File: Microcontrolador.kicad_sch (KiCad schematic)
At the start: 2 parts, among them J2 Conn_01x15, J3 Conn_01x15

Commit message: Inicio de trazado de PCB
Se empezaron a acomodar los footprints.
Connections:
- net Analog_Ilum: now also J2.4 (Pin_4); no longer J2.2 (Pin_2)
- net Analog_pH: now also J2.2 (Pin_2); no longer J2.4 (Pin_4)
- no-connect marks 12 -> 11
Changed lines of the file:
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@@
   (no_connect (at 243.84 97.155))
   (no_connect (at 243.84 92.075))
-  (no_connect (at 243.84 109.855))
   (no_connect (at 215.9 84.455))
   (no_connect (at 243.84 94.615))
@@
     (stroke (width 0) (type default) (color 0 0 0 0))
   )
+  (wire (pts (xy 212.09 76.835) (xy 215.9 76.835))
+    (stroke (width 0) (type default) (color 0 0 0 0))
+  )
+  (wire (pts (xy 109.855 78.74) (xy 128.6002 78.7146))
+    (stroke (width 0) (type default) (color 0 0 0 0))
+  )
+  (wire (pts (xy 215.9 89.535) (xy 200.66 89.535))
+    (stroke (width 0) (type default) (color 0 0 0 0))
+  )
+  (wire (pts (xy 212.09 79.375) (xy 215.9 79.375))
+    (stroke (width 0) (type default) (color 0 0 0 0))
+  )
+  (wire (pts (xy 109.855 69.215) (xy 130.175 69.215))
+    (stroke (width 0) (type default) (color 0 0 0 0))
+  )
+  (wire (pts (xy 208.28 107.315) (xy 215.9 107.315))
+    (stroke (width 0) (type default) (color 0 0 0 0))
+  )
+  (wire (pts (xy 215.9 92.075) (xy 200.66 92.075))
+    (stroke (width 0) (type default) (color 0 0 0 0))
+  )
+  (wire (pts (xy 109.22 118.745) (xy 124.46 118.745))
+    (stroke (width 0) (type default) (color 0 0 0 0))
+  )
+  (wire (pts (xy 109.22 132.715) (xy 121.285 132.715))
+    (stroke (width 0) (type default) (color 0 0 0 0))
+  )
+  (wire (pts (xy 215.9 104.775) (xy 200.66 104.775))
+    (stroke (width 0) (type default) (color 0 0 0 0))
+  )
+  (wire (pts (xy 113.665 59.69) (xy 109.855 59.69))
+    (stroke (width 0) (type default) (color 0 0 0 0))
+  )
+  (wire (pts (xy 59.055 148.59) (xy 62.865 148.59))
+    (stroke (width 0) (type default) (color 0 0 0 0))
+  )
+  (wire (pts (xy 113.665 57.785) (xy 109.855 57.785))
+    (stroke (width 0) (type default) (color 0 0 0 0))
+  )
+  (wire (pts (xy 247.65 99.695) (xy 243.84 99.695))
+    (stroke (width 0) (type default) (color 0 0 0 0))
+  )
+  (wire (pts (xy 59.055 146.685) (xy 62.865 146.685))
+    (stroke (width 0) (type default) (color 0 0 0 0))
+  )
+  (wire (pts (xy 243.84 74.295) (xy 262.5852 74.2696))
+    (stroke (width 0) (type default) (color 0 0 0 0))
+  )
+  (wire (pts (xy 243.84 76.835) (xy 260.35 76.835))
+    (stroke (width 0) (type default) (color 0 0 0 0))
+  )
+  (wire (pts (xy 113.665 55.88) (xy 109.855 55.88))
+    (stroke (width 0) (type default) (color 0 0 0 0))
+  )
+  (wire (pts (xy 109.22 116.84) (xy 124.46 116.84))
+    (stroke (width 0) (type default) (color 0 0 0 0))
+  )
+  (wire (pts (xy 113.665 61.595) (xy 109.855 61.595))
+    (stroke (width 0) (type default) (color 0 0 0 0))
+  )
+  (wire (pts (xy 109.22 120.65) (xy 124.46 120.65))
+    (stroke (width 0) (type default) (color 0 0 0 0))
+  )
+  (wire (pts (xy 215.9 102.235) (xy 200.66 102.235))
+    (stroke (width 0) (type default) (color 0 0 0 0))
+  )
+  (wire (pts (xy 243.84 84.455) (xy 260.35 84.455))
+    (stroke (width 0) (type default) (color 0 0 0 0))
+  )
+  (wire (pts (xy 109.855 76.835) (xy 126.365 76.835))
+    (stroke (width 0) (type default) (color 0 0 0 0))
+  )
+  (wire (pts (xy 59.055 118.745) (xy 62.865 118.745))
+    (stroke (width 0) (type default) (color 0 0 0 0))
+  )
+  (wire (pts (xy 59.055 132.715) (xy 62.865 132.715))
+    (stroke (width 0) (type default) (color 0 0 0 0))
+  )
+  (wire (pts (xy 109.22 124.46) (xy 124.46 124.46))
+    (stroke (width 0) (type default) (color 0 0 0 0))
+  )
+  (wire (pts (xy 59.055 124.46) (xy 62.865 124.46))
+    (stroke (width 0) (type default) (color 0 0 0 0))
+  )
+  (wire (pts (xy 109.22 122.555) (xy 124.46 122.555))
+    (stroke (width 0) (type default) (color 0 0 0 0))
+  )
+  (polyline (pts (xy 176.9618 12.0396) (xy 176.9618 166.0144))
+    (stroke (width 0) (type default) (color 0 0 0 0))
+  )
+  (wire (pts (xy 59.055 116.84) (xy 62.865 116.84))
+    (stroke (width 0) (type default) (color 0 0 0 0))
+  )
+  (wire (pts (xy 109.22 140.97) (xy 122.1486 140.97))
+    (stroke (width 0) (type default) (color 0 0 0 0))
+  )
+  (wire (pts (xy 215.9 94.615) (xy 200.66 94.615))
+    (stroke (width 0) (type default) (color 0 0 0 0))
+  )
+  (wire (pts (xy 59.055 120.65) (xy 62.865 120.65))
+    (stroke (width 0) (type default) (color 0 0 0 0))
+  )
+  (wire (pts (xy 109.22 139.065) (xy 121.285 139.065))
+    (stroke (width 0) (type default) (color 0 0 0 0))
+  )
+  (wire (pts (xy 59.055 150.495) (xy 62.865 150.495))
+    (stroke (width 0) (type default) (color 0 0 0 0))
+  )
+  (wire (pts (xy 59.055 139.065) (xy 62.865 139.065))
+    (stroke (width 0) (type default) (color 0 0 0 0))
+  )
   (wire (pts (xy 212.09 81.915) (xy 215.9 81.915))
-    (stroke (width 0) (type default) (color 0 0 0 0))
-  )
-  (wire (pts (xy 109.855 78.74) (xy 128.6002 78.7146))
-    (stroke (width 0) (type default) (color 0 0 0 0))
-  )
-  (wire (pts (xy 215.9 89.535) (xy 200.66 89.535))
-    (stroke (width 0) (type default) (color 0 0 0 0))
-  )
-  (wire (pts (xy 212.09 79.375) (xy 215.9 79.375))
-    (stroke (width 0) (type default) (color 0 0 0 0))
-  )
-  (wire (pts (xy 109.855 69.215) (xy 130.175 69.215))
-    (stroke (width 0) (type default) (color 0 0 0 0))
-  )
-  (wire (pts (xy 208.28 107.315) (xy 215.9 107.315))
-    (stroke (width 0) (type default) (color 0 0 0 0))
-  )
-  (wire (pts (xy 215.9 92.075) (xy 200.66 92.075))
-    (stroke (width 0) (type default) (color 0 0 0 0))
-  )
-  (wire (pts (xy 109.22 118.745) (xy 124.46 118.745))
-    (stroke (width 0) (type default) (color 0 0 0 0))
-  )
-  (wire (pts (xy 109.22 132.715) (xy 121.285 132.715))
-    (stroke (width 0) (type default) (color 0 0 0 0))
-  )
-  (wire (pts (xy 215.9 104.775) (xy 200.66 104.775))
-    (stroke (width 0) (type default) (color 0 0 0 0))
-  )
-  (wire (pts (xy 113.665 59.69) (xy 109.855 59.69))
-    (stroke (width 0) (type default) (color 0 0 0 0))
-  )
-  (wire (pts (xy 59.055 148.59) (xy 62.865 148.59))
-    (stroke (width 0) (type default) (color 0 0 0 0))
-  )
-  (wire (pts (xy 113.665 57.785) (xy 109.855 57.785))
-    (stroke (width 0) (type default) (color 0 0 0 0))
-  )
-  (wire (pts (xy 247.65 99.695) (xy 243.84 99.695))
-    (stroke (width 0) (type default) (color 0 0 0 0))
-  )
-  (wire (pts (xy 59.055 146.685) (xy 62.865 146.685))
-    (stroke (width 0) (type default) (color 0 0 0 0))
-  )
-  (wire (pts (xy 243.84 74.295) (xy 262.5852 74.2696))
-    (stroke (width 0) (type default) (color 0 0 0 0))
-  )
-  (wire (pts (xy 243.84 76.835) (xy 260.35 76.835))
-    (stroke (width 0) (type default) (color 0 0 0 0))
-  )
-  (wire (pts (xy 113.665 55.88) (xy 109.855 55.88))
-    (stroke (width 0) (type default) (color 0 0 0 0))
-  )
-  (wire (pts (xy 109.22 116.84) (xy 124.46 116.84))
-    (stroke (width 0) (type default) (color 0 0 0 0))
-  )
-  (wire (pts (xy 113.665 61.595) (xy 109.855 61.595))
-    (stroke (width 0) (type default) (color 0 0 0 0))
-  )
-  (wire (pts (xy 109.22 120.65) (xy 124.46 120.65))
-    (stroke (width 0) (type default) (color 0 0 0 0))
-  )
-  (wire (pts (xy 215.9 102.235) (xy 200.66 102.235))
-    (stroke (width 0) (type default) (color 0 0 0 0))
-  )
-  (wire (pts (xy 243.84 84.455) (xy 260.35 84.455))
-    (stroke (width 0) (type default) (color 0 0 0 0))
-  )
-  (wire (pts (xy 109.855 76.835) (xy 126.365 76.835))
-    (stroke (width 0) (type default) (color 0 0 0 0))
-  )
-  (wire (pts (xy 59.055 118.745) (xy 62.865 118.745))
-    (stroke (width 0) (type default) (color 0 0 0 0))
-  )
-  (wire (pts (xy 59.055 132.715) (xy 62.865 132.715))
-    (stroke (width 0) (type default) (color 0 0 0 0))
-  )
-  (wire (pts (xy 109.22 124.46) (xy 124.46 124.46))
-    (stroke (width 0) (type default) (color 0 0 0 0))
-  )
-  (wire (pts (xy 59.055 124.46) (xy 62.865 124.46))
-    (stroke (width 0) (type default) (color 0 0 0 0))
-  )
-  (wire (pts (xy 109.22 122.555) (xy 124.46 122.555))
-    (stroke (width 0) (type default) (color 0 0 0 0))
-  )
-  (polyline (pts (xy 176.9618 12.0396) (xy 176.9618 166.0144))
-    (stroke (width 0) (type default) (color 0 0 0 0))
-  )
-  (wire (pts (xy 59.055 116.84) (xy 62.865 116.84))
-    (stroke (width 0) (type default) (color 0 0 0 0))
-  )
-  (wire (pts (xy 109.22 140.97) (xy 122.1486 140.97))
-    (stroke (width 0) (type default) (color 0 0 0 0))
-  )
-  (wire (pts (xy 215.9 94.615) (xy 200.66 94.615))
-    (stroke (width 0) (type default) (color 0 0 0 0))
-  )
-  (wire (pts (xy 59.055 120.65) (xy 62.865 120.65))
-    (stroke (width 0) (type default) (color 0 0 0 0))
-  )
-  (wire (pts (xy 109.22 139.065) (xy 121.285 139.065))
-    (stroke (width 0) (type default) (color 0 0 0 0))
-  )
-  (wire (pts (xy 59.055 150.495) (xy 62.865 150.495))
-    (stroke (width 0) (type default) (color 0 0 0 0))
-  )
-  (wire (pts (xy 59.055 139.065) (xy 62.865 139.065))
-    (stroke (width 0) (type default) (color 0 0 0 0))
-  )
-  (wire (pts (xy 212.09 76.835) (xy 215.9 76.835))
     (stroke (width 0) (type default) (color 0 0 0 0))
   )
@@
     (effects (font (size 1.27 1.27)) (justify left))
   )
-  (hierarchical_label "Analog_Ilum" (shape input) (at 212.09 76.835 180)
+  (hierarchical_label "Analog_Ilum" (shape input) (at 212.09 81.915 180)
     (effects (font (size 1.27 1.27)) (justify right))
   )
@@
     (effects (font (size 1.27 1.27)) (justify left))
   )
+  (hierarchical_label "+3,3V" (shape input) (at 251.46 109.855 0)
+    (effects (font (size 1.27 1.27)) (justify left))
+  )
   (hierarchical_label "SensorNivel_3_Data" (shape bidirectional) (at 59.055 120.65 180)
     (effects (font (size 1.27 1.27)) (justify right))
@@
     (effects (font (size 1.27 1.27)) (justify left))
   )
-  (hierarchical_label "Analog_pH" (shape input) (at 212.09 81.915 180)
-    (effects (font (size 1.27 1.27)) (justify right))
-  )
+  (hierarchical_label "Analog_pH" (shape input) (at 212.09 76.835 180)
+    (effects (font (size 1.27 1.27)) (justify right))
+  )

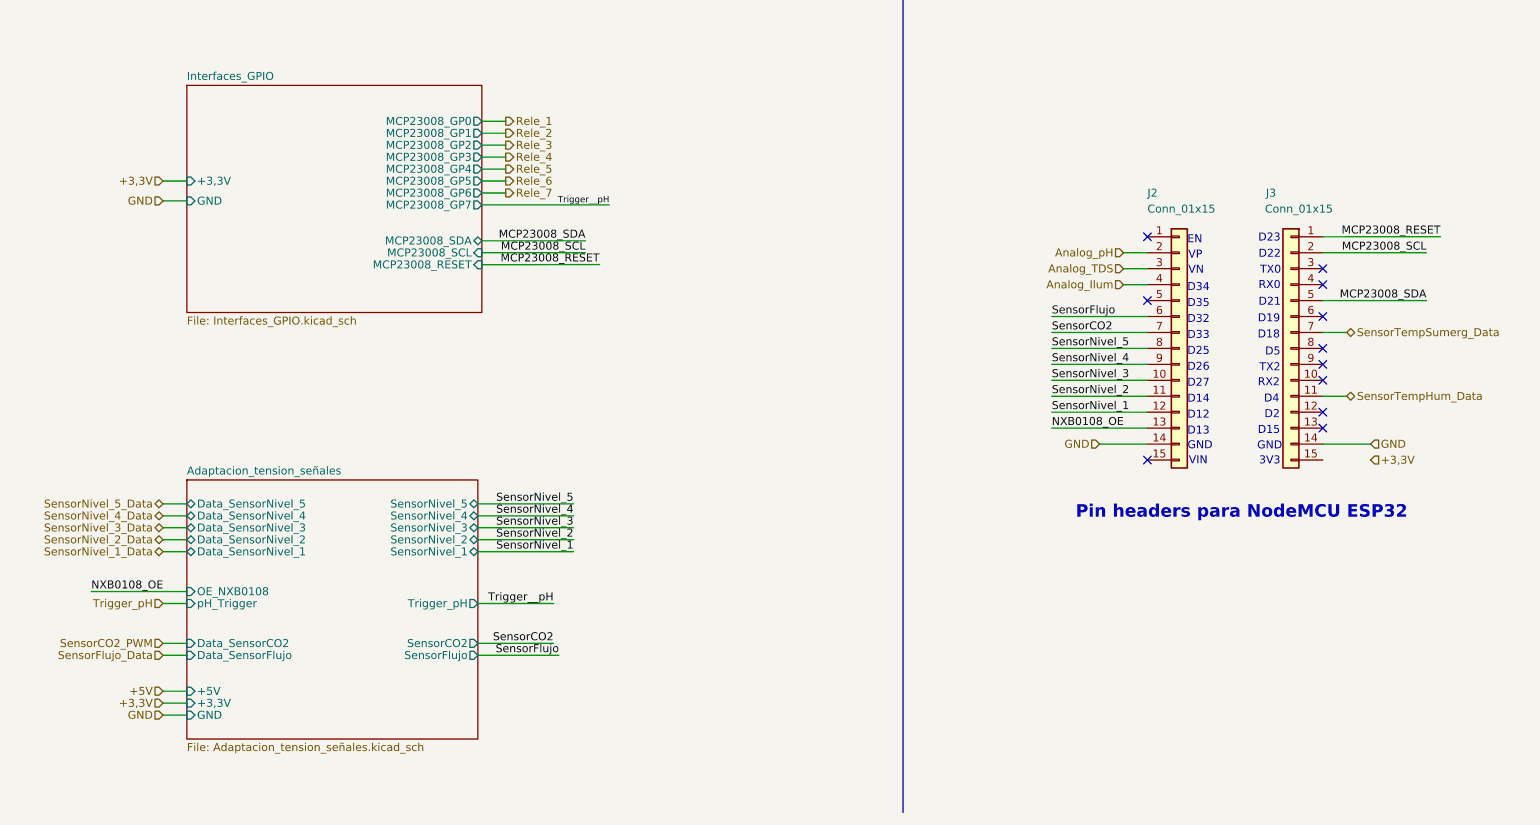
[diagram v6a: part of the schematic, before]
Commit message: Cambios en SCH y PCB.
Se cambio el adaptador de nivel 5-3,3V por un circuito con MOSFET 2N7002, dado que ya no hay stock del NXB. Se modificó el footprint del expansor I/O por uno thorugh-hole.
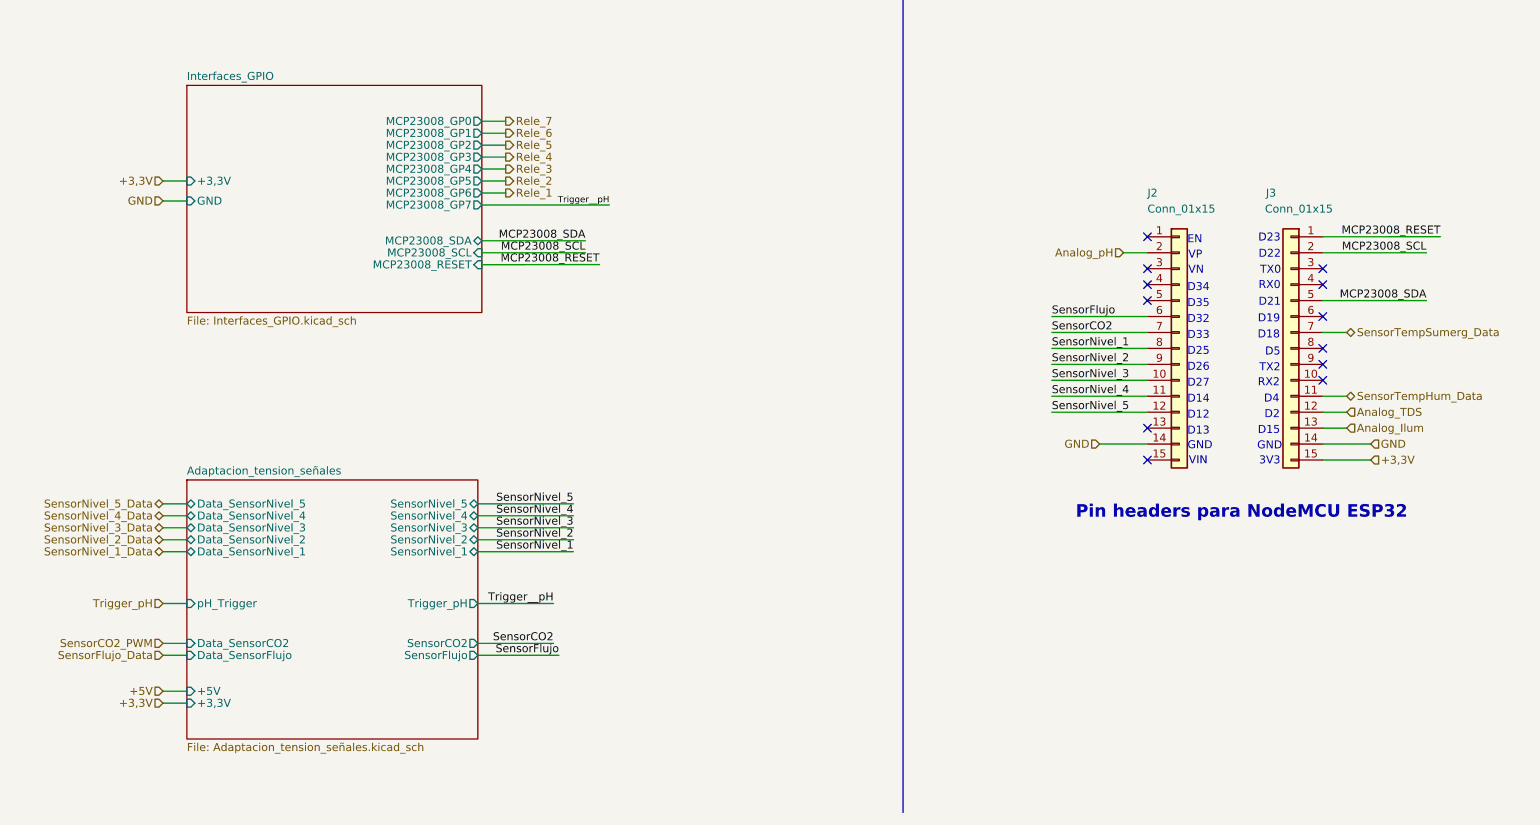
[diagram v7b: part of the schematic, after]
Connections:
- net +3,3V: now also J3.15 (Pin_15)
- net Analog_Ilum: now also J3.13 (Pin_13); no longer J2.4 (Pin_4)
- net Analog_TDS: now also J3.12 (Pin_12); no longer J2.3 (Pin_3)
- net SensorNivel_1: now also J2.8 (Pin_8); no longer J2.12 (Pin_12)
- net SensorNivel_2: now also J2.9 (Pin_9); no longer J2.11 (Pin_11)
- net SensorNivel_4: now also J2.11 (Pin_11); no longer J2.9 (Pin_9)
- net SensorNivel_5: now also J2.12 (Pin_12); no longer J2.8 (Pin_8)
- net NXB0108_OE: no longer names the net of J2.13 (Pin_13)
- no-connect marks 11 -> 12
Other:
- sheet Adaptacion_tension_señales ports: added none; removed GND, OE_NXB0108

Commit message: Finalización de rerouteo de PCB.
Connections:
- net SensorNivel_1: now also J2.12 (Pin_12); no longer J2.8 (Pin_8)
- net SensorNivel_2: now also J2.11 (Pin_11); no longer J2.9 (Pin_9)
- net SensorNivel_4: now also J2.9 (Pin_9); no longer J2.11 (Pin_11)
- net SensorNivel_5: now also J2.8 (Pin_8); no longer J2.12 (Pin_12)
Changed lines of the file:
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@@
     (effects (font (size 1.27 1.27)) (justify right bottom))
   )
-  (label "SensorNivel_4" (at 200.66 99.695 0)
+  (label "SensorNivel_2" (at 200.66 99.695 0)
     (effects (font (size 1.27 1.27)) (justify left bottom))
   )
@@
     (effects (font (size 1.27 1.27)) (justify left bottom))
   )
-  (label "SensorNivel_1" (at 200.66 92.075 0)
+  (label "SensorNivel_5" (at 200.66 92.075 0)
     (effects (font (size 1.27 1.27)) (justify left bottom))
   )
@@
     (effects (font (size 1.27 1.27)) (justify right bottom))
   )
-  (label "SensorNivel_2" (at 200.66 94.615 0)
+  (label "SensorNivel_4" (at 200.66 94.615 0)
     (effects (font (size 1.27 1.27)) (justify left bottom))
   )
@@
     (effects (font (size 1.27 1.27)) (justify right bottom))
   )
-  (label "SensorNivel_5" (at 200.66 102.235 0)
+  (label "SensorNivel_1" (at 200.66 102.235 0)
     (effects (font (size 1.27 1.27)) (justify left bottom))
   )
@@
     (effects (font (size 1.27 1.27)) (justify right))
   )
-  (hierarchical_label "Rele_3" (shape output) (at 113.665 63.5 0)
+  (hierarchical_label "Rele_3" (shape output) (at 113.665 59.69 0)
     (effects (font (size 1.27 1.27)) (justify left))
   )
@@
     (effects (font (size 1.27 1.27)) (justify left))
   )
-  (hierarchical_label "Rele_6" (shape output) (at 113.665 57.785 0)
+  (hierarchical_label "Rele_6" (shape output) (at 113.665 65.405 0)
     (effects (font (size 1.27 1.27)) (justify left))
   )
@@
     (effects (font (size 1.27 1.27)) (justify right))
   )
-  (hierarchical_label "Rele_1" (shape output) (at 113.665 67.31 0)
+  (hierarchical_label "Rele_1" (shape output) (at 113.665 55.88 0)
     (effects (font (size 1.27 1.27)) (justify left))
   )
@@
     (effects (font (size 1.27 1.27)) (justify right))
   )
-  (hierarchical_label "Rele_2" (shape output) (at 113.665 65.405 0)
+  (hierarchical_label "Rele_2" (shape output) (at 113.665 57.785 0)
     (effects (font (size 1.27 1.27)) (justify left))
   )
-  (hierarchical_label "Rele_7" (shape output) (at 113.665 55.88 0)
+  (hierarchical_label "Rele_7" (shape output) (at 113.665 67.31 0)
     (effects (font (size 1.27 1.27)) (justify left))
   )
-  (hierarchical_label "Rele_5" (shape output) (at 113.665 59.69 0)
+  (hierarchical_label "Rele_5" (shape output) (at 113.665 63.5 0)
     (effects (font (size 1.27 1.27)) (justify left))
   )
